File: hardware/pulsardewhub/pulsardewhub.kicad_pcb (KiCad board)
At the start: 4 copper layers, 180 x 110 mm, 222 parts, among them J1 SWD, J10 XT60: 2=PLUS, 1=GND, J101 5A DC / center +, J11 BARREL input / DNP, J201 5A DC / center +, J301 5A DC / center +, J40 USB-C upstream, J401 5A DC / center +, J501 USB-A / 500mA, J51 HEATER 1, J601 USB-A / 500mA, J61 HEATER 2, J701 USB-A / 500mA, J801 USB-A / 500mA, Q10 CSD18540Q5B, Q51 AOD4184A, Q61 AOD4184A, U1 STM32G0B1KBU6, U10 LM74700QDBV, U101 TPS26631PWP, U2 SHT40-AD1B-R2, U20 LMR33630ADDA, U201 TPS26631PWP, U30 LMR33630ADDA, U301 TPS26631PWP, U40 USB2517-JZX, U401 TPS26631PWP, U41 TPS3808G33DBV, U42 USBLC6-2SC6, U50 TC4427AVOA713, U501 TPS2553DBV, U502 USBLC6-2SC6, U51 INA226, U601 TPS2553DBV, U602 USBLC6-2SC6, U701 TPS2553DBV, U702 USBLC6-2SC6, U801 TPS2553DBV, U802 USBLC6-2SC6, Y40 24MHz / CL=12pF

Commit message: Use TPS259827 high-side switches for 12–18 V DC outlets
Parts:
- removed R111, R211, R311, R411: 22k, Resistor_SMD:R_0603_1608Metric
- added C105: 100n, Capacitor_SMD:C_0603_1608Metric, F.Cu at (120.0, 140.0)
- added C205: 100n, Capacitor_SMD:C_0603_1608Metric, F.Cu at (148.0, 140.0)
- added C305: 100n, Capacitor_SMD:C_0603_1608Metric, F.Cu at (176.0, 140.0)
- added C405: 100n, Capacitor_SMD:C_0603_1608Metric, F.Cu at (204.0, 140.0)
- added D102: SMBJ18A, Diode_SMD:D_SMB, F.Cu at (127.0, 125.0)
- added D202: SMBJ18A, Diode_SMD:D_SMB, F.Cu at (155.0, 125.0)
- added D302: SMBJ18A, Diode_SMD:D_SMB, F.Cu at (183.0, 125.0)
- added D402: SMBJ18A, Diode_SMD:D_SMB, F.Cu at (211.0, 125.0)
- added U102: TPS3700DDC, Package_TO_SOT_SMD:SOT-23-6, F.Cu at (120.0, 137.0)
- added U202: TPS3700DDC, Package_TO_SOT_SMD:SOT-23-6, F.Cu at (148.0, 137.0)
- added U302: TPS3700DDC, Package_TO_SOT_SMD:SOT-23-6, F.Cu at (176.0, 137.0)
- added U402: TPS3700DDC, Package_TO_SOT_SMD:SOT-23-6, F.Cu at (204.0, 137.0)
- C103, C203, C303, C403: value 22n / 50V -> 4.7n / 50V
- D10: value SMCJ20A -> SMCJ18A
- D101, D201, D301, D401: value SMBJ20A -> SS54; footprint Diode_SMD:D_SMB -> Diode_SMD:D_SMA
- R101, R201, R301, R401: value 150k -> 220k
- R102, R202, R302, R402: value 22k -> 10k
- R103, R203, R303, R403: value 332k -> 470k
- R104, R204, R304, R404: value 20k -> 10k
- R105, R205, R305, R405: value 10k -> 100k
- R107, R207, R307, R407: value 3.3k / 1% -> 249 / 1%
- R108, R208, R308, R408: value 8.2k / 1% -> 820 / 1%
- R109, R209, R309, R409: value 1k -> 10k
- R110, R210, R310, R410: value 150k -> 10k
- U101, U201, U301, U401: value TPS26631PWP -> TPS259827ONRGE; footprint pulsarfab:TI_PWP0020T_EP2.96x2.96mm -> pulsarfab:TI_RGE0024M_VQFN24_2EP_4x4mm
- moved R110 9.06 mm to (124.0, 140.0)
- moved R210 9.06 mm to (152.0, 140.0)
- moved R310 9.06 mm to (180.0, 140.0)
- moved R410 9.06 mm to (208.0, 140.0)
- moved C103 7.81 mm to (132.0, 134.0), turned to 90 degrees
- moved C203 7.81 mm to (160.0, 134.0), turned to 90 degrees
- moved C303 7.81 mm to (188.0, 134.0), turned to 90 degrees
- moved C403 7.81 mm to (216.0, 134.0), turned to 90 degrees
- moved R108 5.83 mm to (133.0, 137.0)
- moved R208 5.83 mm to (161.0, 137.0)
- moved R308 5.83 mm to (189.0, 137.0)
- moved R408 5.83 mm to (217.0, 137.0)
- moved R105 4.00 mm to (124.0, 137.0)
- moved R205 4.00 mm to (152.0, 137.0)
- moved R305 4.00 mm to (180.0, 137.0)
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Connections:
- R101 pad 2: /DC outlet 1/UVLO -> /DC outlet 1/UV_SENSE
- R102 pad 1: /DC outlet 1/UVLO -> /DC outlet 1/UV_SENSE
- R103 pad 2: /DC outlet 1/OVP -> /DC outlet 1/OV_SENSE
- R104 pad 1: /DC outlet 1/OVP -> /DC outlet 1/OV_SENSE
- R105 pad 1: /DC_EN1 -> /DC outlet 1/EN_SW
- R106 pad 2: /DC_FLT1 -> /DC_PG1
- R110 pad 1: /DC outlet 1/OUT -> /DC_EN1
- R110 pad 2: /DC outlet 1/PGTH -> /DC outlet 1/EN_SW
- R201 pad 2: /DC outlet 2/UVLO -> /DC outlet 2/UV_SENSE
- R202 pad 1: /DC outlet 2/UVLO -> /DC outlet 2/UV_SENSE
- R203 pad 2: /DC outlet 2/OVP -> /DC outlet 2/OV_SENSE
- R204 pad 1: /DC outlet 2/OVP -> /DC outlet 2/OV_SENSE
- R205 pad 1: /DC_EN2 -> /DC outlet 2/EN_SW
- R206 pad 2: /DC_FLT2 -> /DC_PG2
- R210 pad 1: /DC outlet 2/OUT -> /DC_EN2
- R210 pad 2: /DC outlet 2/PGTH -> /DC outlet 2/EN_SW
- R301 pad 2: /DC outlet 3/UVLO -> /DC outlet 3/UV_SENSE
- R302 pad 1: /DC outlet 3/UVLO -> /DC outlet 3/UV_SENSE
- R303 pad 2: /DC outlet 3/OVP -> /DC outlet 3/OV_SENSE
- R304 pad 1: /DC outlet 3/OVP -> /DC outlet 3/OV_SENSE
- R305 pad 1: /DC_EN3 -> /DC outlet 3/EN_SW
- R306 pad 2: /DC_FLT3 -> /DC_PG3
- R310 pad 1: /DC outlet 3/OUT -> /DC_EN3
- R310 pad 2: /DC outlet 3/PGTH -> /DC outlet 3/EN_SW
- R401 pad 2: /DC outlet 4/UVLO -> /DC outlet 4/UV_SENSE
- R402 pad 1: /DC outlet 4/UVLO -> /DC outlet 4/UV_SENSE
- R403 pad 2: /DC outlet 4/OVP -> /DC outlet 4/OV_SENSE
- R404 pad 1: /DC outlet 4/OVP -> /DC outlet 4/OV_SENSE
- R405 pad 1: /DC_EN4 -> /DC outlet 4/EN_SW
- R406 pad 2: /DC_FLT4 -> /DC_PG4
- R410 pad 1: /DC outlet 4/OUT -> /DC_EN4
- R410 pad 2: /DC outlet 4/PGTH -> /DC outlet 4/EN_SW
- U1 pad 20: /DC_FLT4 -> /DC_PG4
- U1 pad 27: /DC_FLT1 -> /DC_PG1
- U1 pad 28: /DC_FLT2 -> /DC_PG2
- U1 pad 29: /DC_FLT3 -> /DC_PG3
- U101 pad 10: /DC outlet 1/DVDT -> /GND
- U101 pad 11: /DC outlet 1/ILIM -> /GND
- U101 pad 12: unconnected-(U101-MODE-Pad12) -> /GND
- U101 pad 13: /DC_EN1 -> /DC_PG1
- U101 pad 14: /DC outlet 1/IMON_RAW -> /GND
- U101 pad 15: /DC_FLT1 -> /DC outlet 1/DVDT
- U101 pad 16: /DC outlet 1/PGTH -> /VIN
- U101 pad 17: unconnected-(U101-PGOOD-Pad17) -> /DC outlet 1/OUT
- U101 pad 21: /GND -> /DC outlet 1/OUT
- U101 pad 4: unconnected-(U101-B_GATE-Pad4) -> /GND
- U101 pad 5: unconnected-(U101-DRV-Pad5) -> /GND
- U101 pad 6: /VIN -> /DC outlet 1/EN_SW
- U101 pad 7: /DC outlet 1/UVLO -> unconnected-(U101-ITIMER-Pad7)
- U101 pad 8: /DC outlet 1/OVP -> /DC outlet 1/ILIM
- U101 pad 9: /GND -> /DC outlet 1/IMON_RAW
- U201 pad 10: /DC outlet 2/DVDT -> /GND
- U201 pad 11: /DC outlet 2/ILIM -> /GND
- U201 pad 12: unconnected-(U201-MODE-Pad12) -> /GND
- U201 pad 13: /DC_EN2 -> /DC_PG2
- U201 pad 14: /DC outlet 2/IMON_RAW -> /GND
- U201 pad 15: /DC_FLT2 -> /DC outlet 2/DVDT
- U201 pad 16: /DC outlet 2/PGTH -> /VIN
- U201 pad 17: unconnected-(U201-PGOOD-Pad17) -> /DC outlet 2/OUT
- U201 pad 21: /GND -> /DC outlet 2/OUT
- U201 pad 4: unconnected-(U201-B_GATE-Pad4) -> /GND
- U201 pad 5: unconnected-(U201-DRV-Pad5) -> /GND
- U201 pad 6: /VIN -> /DC outlet 2/EN_SW
- U201 pad 7: /DC outlet 2/UVLO -> unconnected-(U201-ITIMER-Pad7)
- U201 pad 8: /DC outlet 2/OVP -> /DC outlet 2/ILIM
- U201 pad 9: /GND -> /DC outlet 2/IMON_RAW
- U301 pad 10: /DC outlet 3/DVDT -> /GND
- U301 pad 11: /DC outlet 3/ILIM -> /GND
- U301 pad 12: unconnected-(U301-MODE-Pad12) -> /GND
- U301 pad 13: /DC_EN3 -> /DC_PG3
- U301 pad 14: /DC outlet 3/IMON_RAW -> /GND
- U301 pad 15: /DC_FLT3 -> /DC outlet 3/DVDT
- U301 pad 16: /DC outlet 3/PGTH -> /VIN
- U301 pad 17: unconnected-(U301-PGOOD-Pad17) -> /DC outlet 3/OUT
- U301 pad 21: /GND -> /DC outlet 3/OUT
- U301 pad 4: unconnected-(U301-B_GATE-Pad4) -> /GND
- U301 pad 5: unconnected-(U301-DRV-Pad5) -> /GND
- U301 pad 6: /VIN -> /DC outlet 3/EN_SW
- U301 pad 7: /DC outlet 3/UVLO -> unconnected-(U301-ITIMER-Pad7)
- U301 pad 8: /DC outlet 3/OVP -> /DC outlet 3/ILIM
- U301 pad 9: /GND -> /DC outlet 3/IMON_RAW
- U401 pad 10: /DC outlet 4/DVDT -> /GND
- U401 pad 11: /DC outlet 4/ILIM -> /GND
- U401 pad 12: unconnected-(U401-MODE-Pad12) -> /GND
- U401 pad 13: /DC_EN4 -> /DC_PG4
- U401 pad 14: /DC outlet 4/IMON_RAW -> /GND
- U401 pad 15: /DC_FLT4 -> /DC outlet 4/DVDT
- U401 pad 16: /DC outlet 4/PGTH -> /VIN
- U401 pad 17: unconnected-(U401-PGOOD-Pad17) -> /DC outlet 4/OUT
- U401 pad 21: /GND -> /DC outlet 4/OUT
- U401 pad 4: unconnected-(U401-B_GATE-Pad4) -> /GND
- U401 pad 5: unconnected-(U401-DRV-Pad5) -> /GND
- U401 pad 6: /VIN -> /DC outlet 4/EN_SW
- U401 pad 7: /DC outlet 4/UVLO -> unconnected-(U401-ITIMER-Pad7)
- U401 pad 8: /DC outlet 4/OVP -> /DC outlet 4/ILIM
- U401 pad 9: /GND -> /DC outlet 4/IMON_RAW
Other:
- board text added: "12-18V IN"
- board text added: "PulsarDew Hub 0.2"
- board text removed: "12-20V IN"
- board text removed: "PulsarDew Hub 0.1"

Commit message: Use economical through-hole USB-A sockets for PulsarPower
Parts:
- J501, J601, J701, J801: footprint pulsarfab:USB_A_GCT_USB1046_Edge -> pulsarfab:USB_A_SHOUHAN_AF90ZJWG_THT
- moved J501 7.00 mm to (124.0, 62.0)
- moved J601 7.00 mm to (148.0, 62.0)
- moved J701 7.00 mm to (172.0, 62.0)
- moved J801 7.00 mm to (196.0, 62.0)

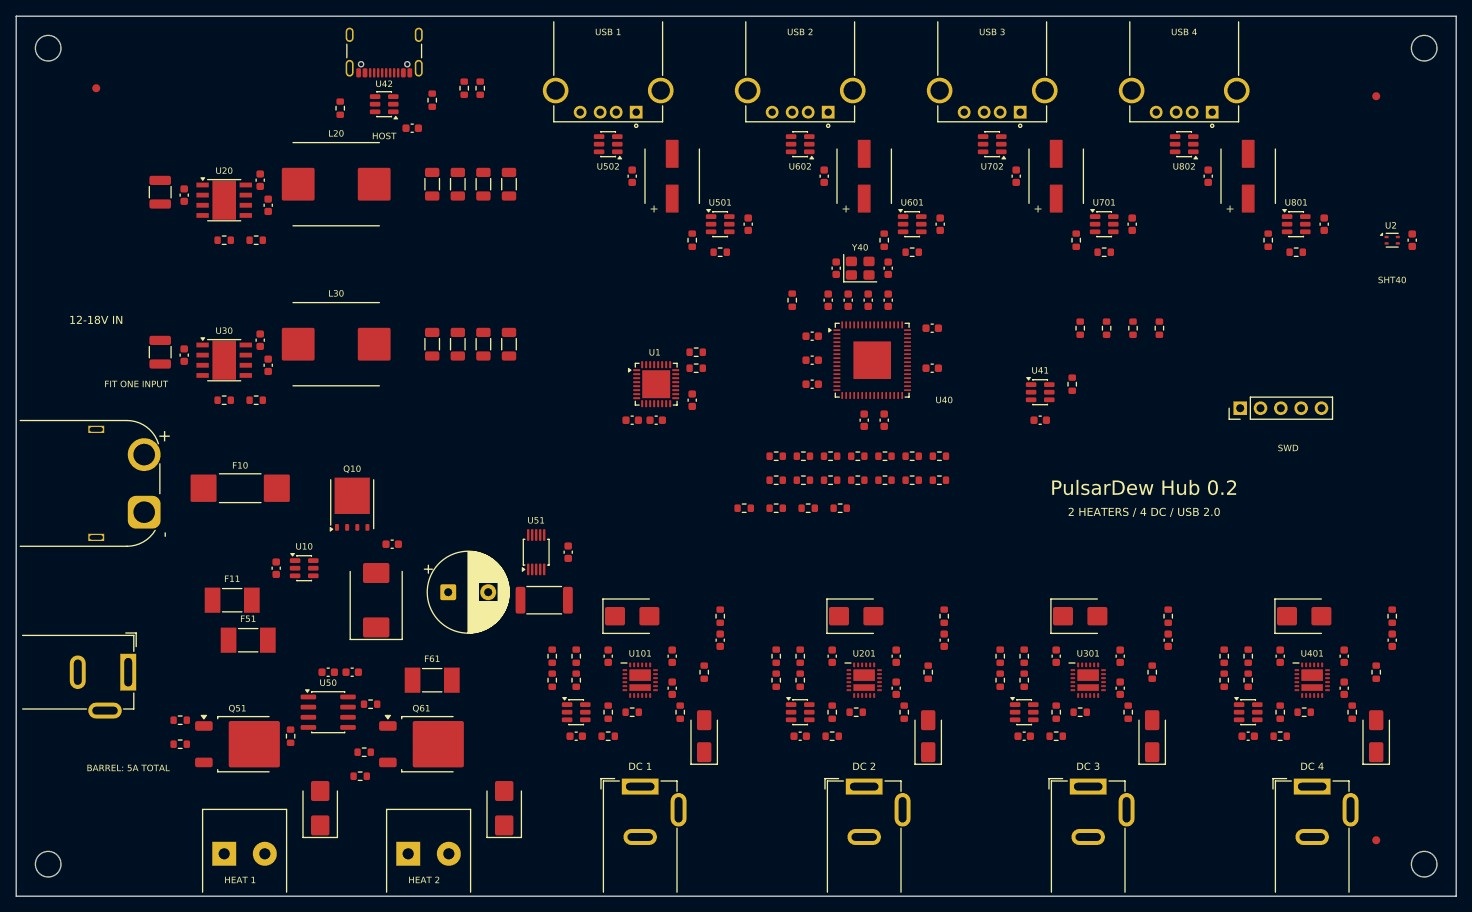
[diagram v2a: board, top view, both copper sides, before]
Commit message: Reduce PulsarPower power-path cost while retaining current monitoring
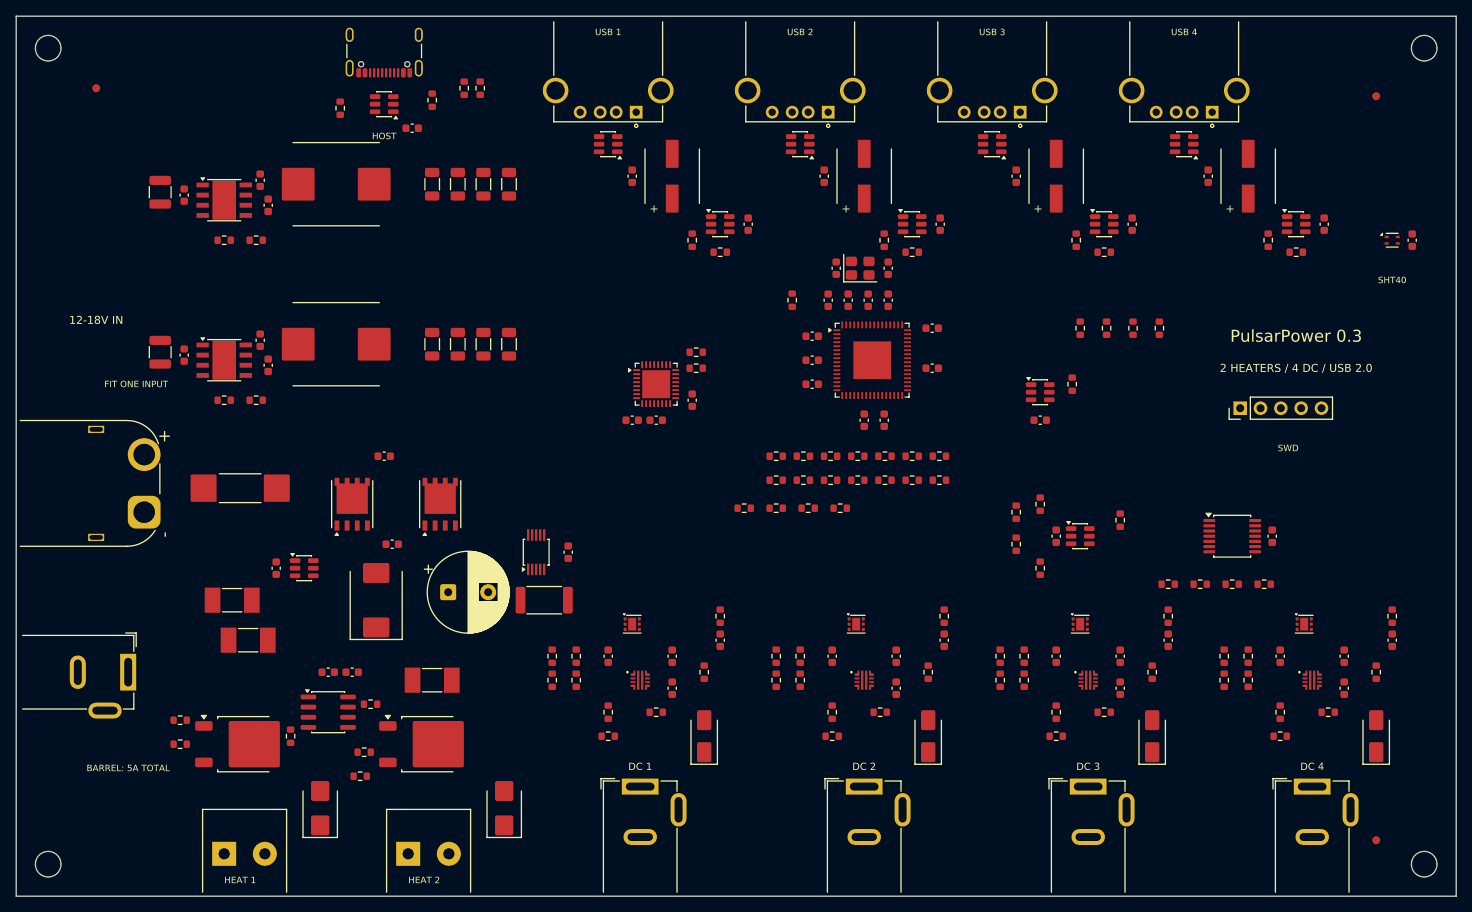
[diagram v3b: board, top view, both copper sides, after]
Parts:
- removed C105, C205, C305, C405: 100n, Capacitor_SMD:C_0603_1608Metric
- removed D102, D202, D302, D402: SMBJ18A, Diode_SMD:D_SMB
- removed R108, R208, R308, R408: 820 / 1%, Resistor_SMD:R_0603_1608Metric
- added C13: 100n / 50V, Capacitor_SMD:C_0603_1608Metric, F.Cu at (96.0, 105.0)
- added C70: 100n, Capacitor_SMD:C_0603_1608Metric, F.Cu at (180.0, 115.0)
- added C71: 100n, Capacitor_SMD:C_0603_1608Metric, F.Cu at (207.0, 115.0)
- added Q11: SiR680LDP, Package_SO:PowerPAK_SO-8_Single, F.Cu at (103.0, 111.0)
- added R70: 220k, Resistor_SMD:R_0603_1608Metric, F.Cu at (175.0, 112.0)
- added R71: 10k, Resistor_SMD:R_0603_1608Metric, F.Cu at (175.0, 116.0)
- added R72: 470k, Resistor_SMD:R_0603_1608Metric, F.Cu at (178.0, 111.0)
- added R73: 10k, Resistor_SMD:R_0603_1608Metric, F.Cu at (178.0, 119.0)
- added R74: 10k, Resistor_SMD:R_0603_1608Metric, F.Cu at (188.0, 113.0)
- added R75: 10k, Resistor_SMD:R_0603_1608Metric, F.Cu at (194.0, 121.0)
- added R76: 10k, Resistor_SMD:R_0603_1608Metric, F.Cu at (198.0, 121.0)
- added R77: 10k, Resistor_SMD:R_0603_1608Metric, F.Cu at (202.0, 121.0)
- added R78: 10k, Resistor_SMD:R_0603_1608Metric, F.Cu at (206.0, 121.0)
- added U70: TPS3700DDC, Package_TO_SOT_SMD:SOT-23-6, F.Cu at (183.0, 115.0)
- added U71: SN74LVC08APW, Package_SO:TSSOP-14_4.4x5mm_P0.65mm, F.Cu at (202.0, 115.0)
- C10: value 100n / 50V -> 1u / 50V
- Q10: value CSD18540Q5B -> SiR680LDP; footprint Package_TO_SOT_SMD:TDSON-8-1 -> Package_SO:PowerPAK_SO-8_Single
- R101, R201, R301, R401: value 220k -> 100k
- R102, R202, R302, R402: value 10k -> 20k
- R103, R203, R303, R403: value 470k -> 150k
- R105, R205, R305, R405: value 100k -> 10k
- R107, R207, R307, R407: value 249 / 1% -> 1k / 1%
- R110, R210, R310, R410: value 10k -> 1k
- U101, U201, U301, U401: value TPS259827ONRGE -> TPS25974LRPW; footprint pulsarfab:TI_RGE0024M_VQFN24_2EP_4x4mm -> pulsarfab:TI_RPW0010A_VQFN10_2x2mm
- U102, U202, U302, U402: value TPS3700DDC -> TVS1800DRV; footprint Package_TO_SOT_SMD:SOT-23-6 -> Package_SON:WSON-6-1EP_2x2mm_P0.65mm_EP1x1.6mm
- moved U102 13.0 mm to (127.0, 126.0)
- moved U202 13.0 mm to (155.0, 126.0)
- moved U302 13.0 mm to (183.0, 126.0)
- moved U402 13.0 mm to (211.0, 126.0)
- moved R107 3.00 mm to (130.0, 137.0)
- moved R207 3.00 mm to (158.0, 137.0)
- moved R307 3.00 mm to (186.0, 137.0)
- moved R407 3.00 mm to (214.0, 137.0)
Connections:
- R101 pad 1: /VIN -> /DC outlet 1/OUT
- R101 pad 2: /DC outlet 1/UV_SENSE -> /DC outlet 1/PG_SENSE
- R102 pad 1: /DC outlet 1/UV_SENSE -> /DC outlet 1/PG_SENSE
- R107 pad 1: /DC outlet 1/ILIM -> /DC outlet 1/IMON_RAW
- R110 pad 1: /DC_EN1 -> /DC_SAFE1
- R201 pad 1: /VIN -> /DC outlet 2/OUT
- R201 pad 2: /DC outlet 2/UV_SENSE -> /DC outlet 2/PG_SENSE
- R202 pad 1: /DC outlet 2/UV_SENSE -> /DC outlet 2/PG_SENSE
- R207 pad 1: /DC outlet 2/ILIM -> /DC outlet 2/IMON_RAW
- R210 pad 1: /DC_EN2 -> /DC_SAFE2
- R301 pad 1: /VIN -> /DC outlet 3/OUT
- R301 pad 2: /DC outlet 3/UV_SENSE -> /DC outlet 3/PG_SENSE
- R302 pad 1: /DC outlet 3/UV_SENSE -> /DC outlet 3/PG_SENSE
- R307 pad 1: /DC outlet 3/ILIM -> /DC outlet 3/IMON_RAW
- R310 pad 1: /DC_EN3 -> /DC_SAFE3
- R401 pad 1: /VIN -> /DC outlet 4/OUT
- R401 pad 2: /DC outlet 4/UV_SENSE -> /DC outlet 4/PG_SENSE
- R402 pad 1: /DC outlet 4/UV_SENSE -> /DC outlet 4/PG_SENSE
- R407 pad 1: /DC outlet 4/ILIM -> /DC outlet 4/IMON_RAW
- R410 pad 1: /DC_EN4 -> /DC_SAFE4
- U101 pad 1: /VIN -> /DC outlet 1/EN_SW
- U101 pad 10: /GND -> unconnected-(U101-ITIMER-Pad10)
- U101 pad 2: /VIN -> /DC outlet 1/OV_SENSE
- U101 pad 3: /VIN -> /DC_PG1
- U101 pad 4: /GND -> /DC outlet 1/PG_SENSE
- U101 pad 5: /GND -> /VIN
- U101 pad 6: /DC outlet 1/EN_SW -> /DC outlet 1/OUT
- U101 pad 7: unconnected-(U101-ITIMER-Pad7) -> /DC outlet 1/DVDT
- U101 pad 8: /DC outlet 1/ILIM -> /GND
- U102 pad 1: /DC outlet 1/EN_SW -> /GND
- U102 pad 3: /DC outlet 1/UV_SENSE -> /GND
- U102 pad 4: /DC outlet 1/OV_SENSE -> /VIN
- U102 pad 5: /V3 -> /VIN
- U102 pad 6: /DC outlet 1/EN_SW -> /VIN
- U201 pad 1: /VIN -> /DC outlet 2/EN_SW
- U201 pad 10: /GND -> unconnected-(U201-ITIMER-Pad10)
- U201 pad 2: /VIN -> /DC outlet 2/OV_SENSE
- U201 pad 3: /VIN -> /DC_PG2
- U201 pad 4: /GND -> /DC outlet 2/PG_SENSE
- U201 pad 5: /GND -> /VIN
- U201 pad 6: /DC outlet 2/EN_SW -> /DC outlet 2/OUT
- U201 pad 7: unconnected-(U201-ITIMER-Pad7) -> /DC outlet 2/DVDT
- U201 pad 8: /DC outlet 2/ILIM -> /GND
- U202 pad 1: /DC outlet 2/EN_SW -> /GND
- U202 pad 3: /DC outlet 2/UV_SENSE -> /GND
- U202 pad 4: /DC outlet 2/OV_SENSE -> /VIN
- U202 pad 5: /V3 -> /VIN
- U202 pad 6: /DC outlet 2/EN_SW -> /VIN
- U301 pad 1: /VIN -> /DC outlet 3/EN_SW
- U301 pad 10: /GND -> unconnected-(U301-ITIMER-Pad10)
- U301 pad 2: /VIN -> /DC outlet 3/OV_SENSE
- U301 pad 3: /VIN -> /DC_PG3
- U301 pad 4: /GND -> /DC outlet 3/PG_SENSE
- U301 pad 5: /GND -> /VIN
- U301 pad 6: /DC outlet 3/EN_SW -> /DC outlet 3/OUT
- U301 pad 7: unconnected-(U301-ITIMER-Pad7) -> /DC outlet 3/DVDT
- U301 pad 8: /DC outlet 3/ILIM -> /GND
- U302 pad 1: /DC outlet 3/EN_SW -> /GND
- U302 pad 3: /DC outlet 3/UV_SENSE -> /GND
- U302 pad 4: /DC outlet 3/OV_SENSE -> /VIN
- U302 pad 5: /V3 -> /VIN
- U302 pad 6: /DC outlet 3/EN_SW -> /VIN
- U401 pad 1: /VIN -> /DC outlet 4/EN_SW
- U401 pad 10: /GND -> unconnected-(U401-ITIMER-Pad10)
- U401 pad 2: /VIN -> /DC outlet 4/OV_SENSE
- U401 pad 3: /VIN -> /DC_PG4
- U401 pad 4: /GND -> /DC outlet 4/PG_SENSE
- U401 pad 5: /GND -> /VIN
- U401 pad 6: /DC outlet 4/EN_SW -> /DC outlet 4/OUT
- U401 pad 7: unconnected-(U401-ITIMER-Pad7) -> /DC outlet 4/DVDT
- U401 pad 8: /DC outlet 4/ILIM -> /GND
- U402 pad 1: /DC outlet 4/EN_SW -> /GND
- U402 pad 3: /DC outlet 4/UV_SENSE -> /GND
- U402 pad 4: /DC outlet 4/OV_SENSE -> /VIN
- U402 pad 5: /V3 -> /VIN
- U402 pad 6: /DC outlet 4/EN_SW -> /VIN
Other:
- board text added: "PulsarPower 0.3"
- board text removed: "PulsarDew Hub 0.2"

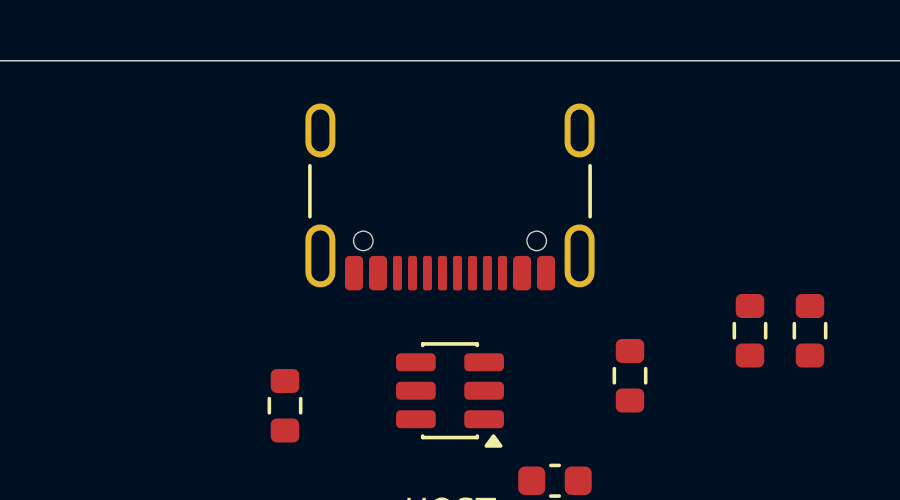
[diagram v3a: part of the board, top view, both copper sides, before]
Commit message: Use stocked HRO USB-C sockets on PulsarPower and PulsarDew
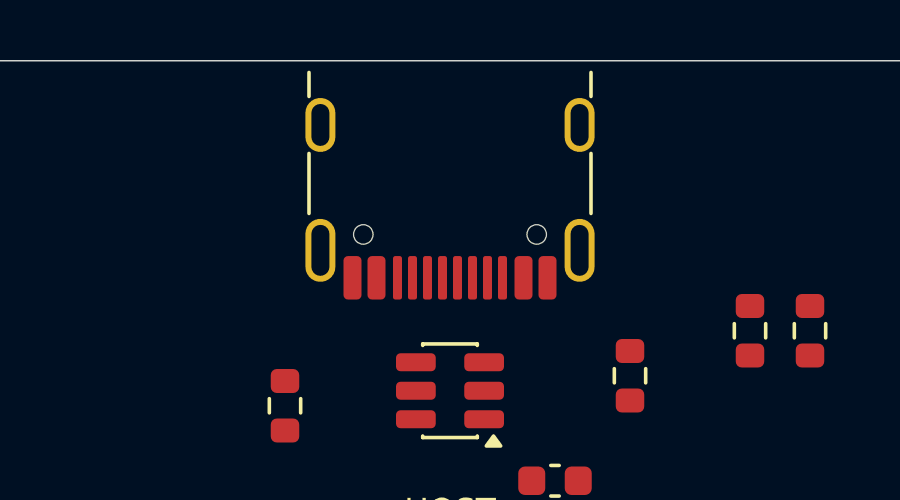
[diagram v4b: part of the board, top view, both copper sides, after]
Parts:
- J40: footprint Connector_USB:USB_C_Receptacle_GCT_USB4105-xx-A_16P_TopMnt_Horizontal -> pulsarfab:USB_C_HRO_TYPE-C-31-M-12
- moved J40 0.21 mm to (96.0, 53.2)

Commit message: Use owned XKB barrel sockets and evaluate LMR51610 commonality
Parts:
- J101, J11, J201, J301, J401: footprint pulsarfab:BarrelJack_GCT_DCJ200_Edge -> pulsarfab:BarrelJack_XKB_DC-005K-5A_Edge
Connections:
- J101 pad 3: unconnected-(J101-Pad3) -> /GND
- J11 pad 3: unconnected-(J11-Pad3) -> /GND
- J201 pad 3: unconnected-(J201-Pad3) -> /GND
- J301 pad 3: unconnected-(J301-Pad3) -> /GND
- J401 pad 3: unconnected-(J401-Pad3) -> /GND
